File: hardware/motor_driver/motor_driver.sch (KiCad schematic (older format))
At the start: 37 parts, among them P1 TERM_BLOCK_CON, P2 JUMPER_CIRC_SUPLLY, P3 TERM_BLOCK_CON, P4 FEMALE_HEADER, P5 MOLEX_HEADER, Q1 IRFZ40, Q2 IRFZ40, Q3 IRFZ40, Q4 IRFZ40, U1 LM7812, U2 LM7805, U3 HIP4081A, U4 SN74S04

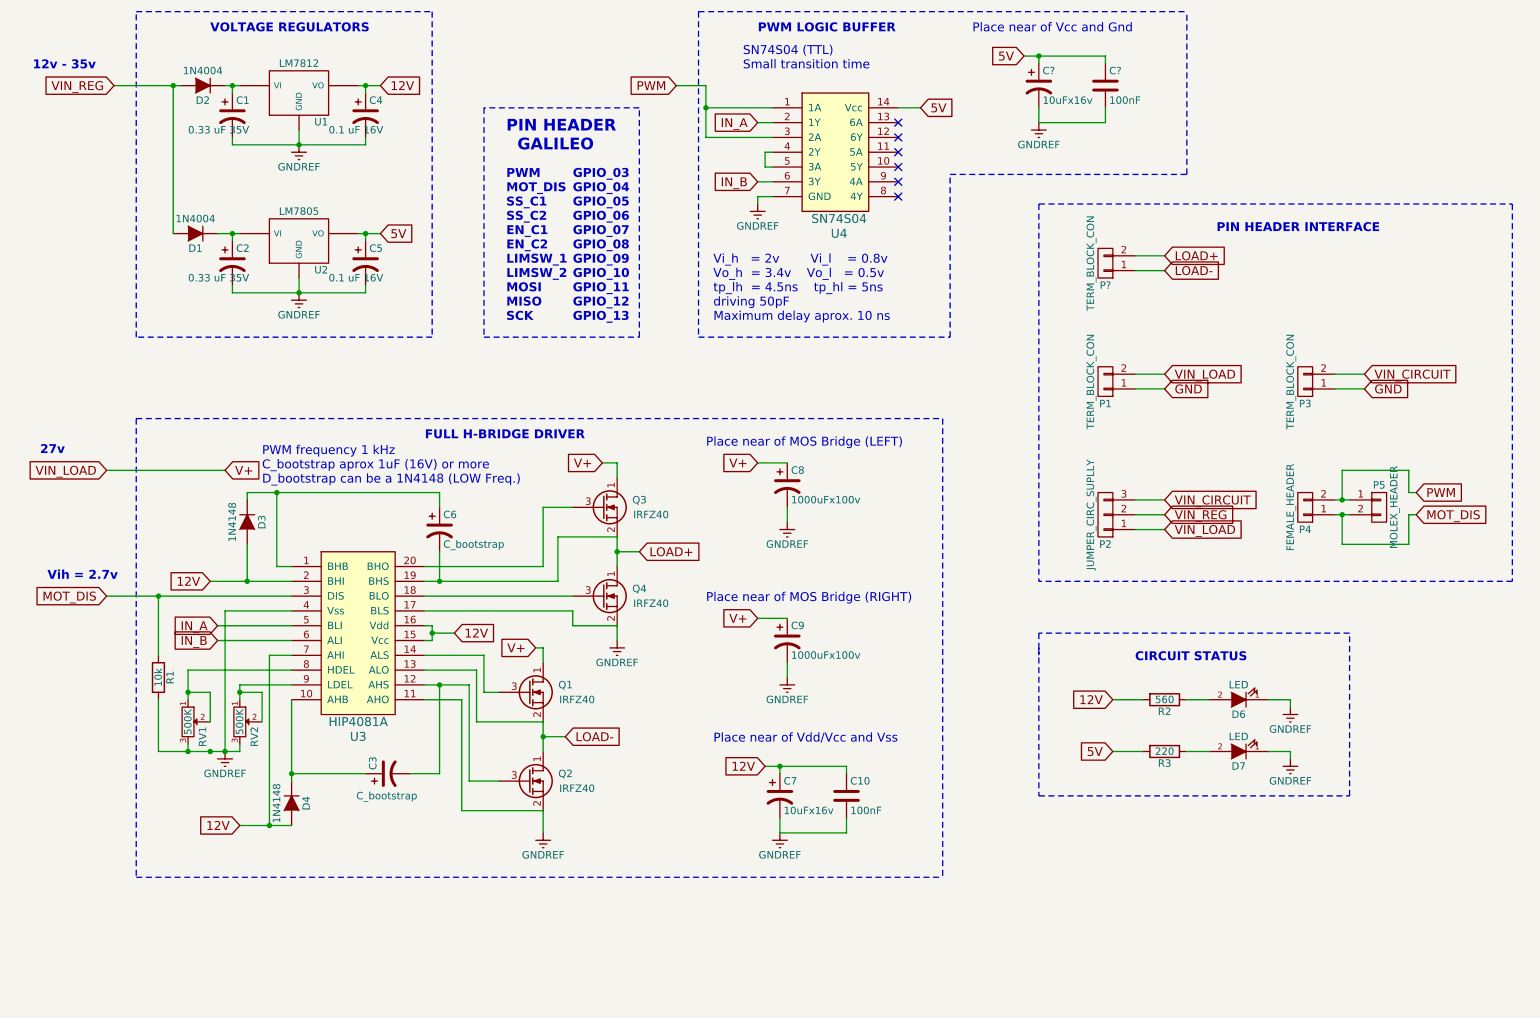
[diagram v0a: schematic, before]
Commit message: Added PID, LS7366R lib and layout off DC Motor Driver PCB and Arduino Shied PCB.
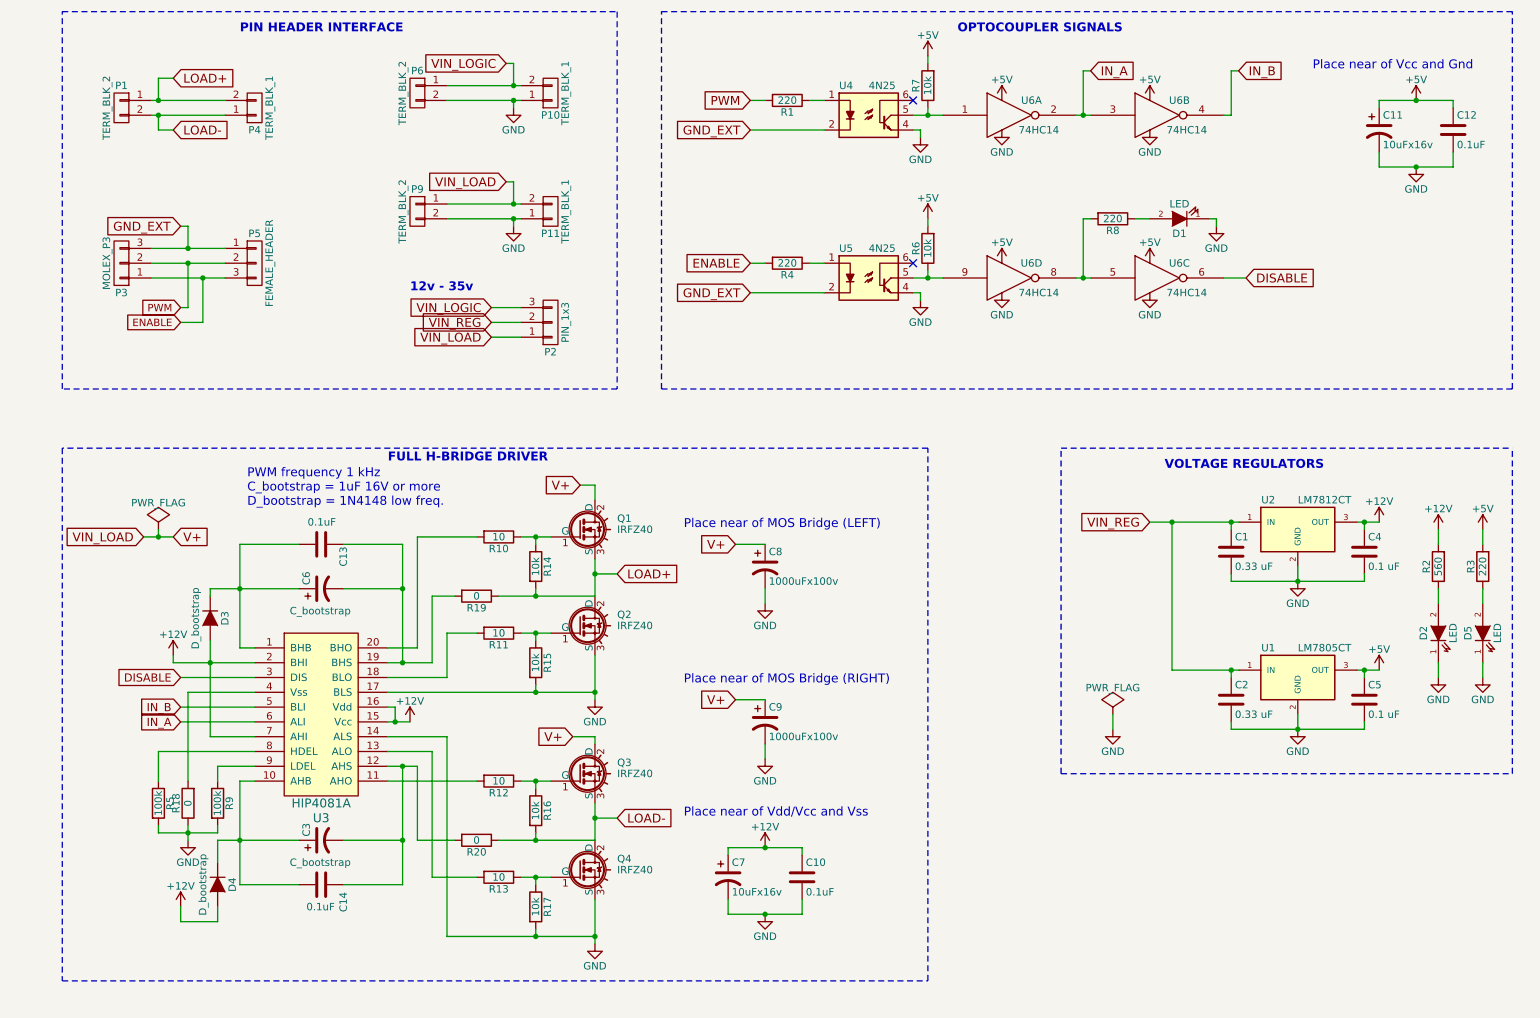
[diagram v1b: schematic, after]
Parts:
- removed C1, C2: 0.33 uF 35V, symbol CP1
- removed C4, C5: 0.1 uF 16V, symbol CP1
- removed D1, D2: 1N4004, symbol D
- removed D6, D7: LED, symbol LED
- removed P3, P?: TERM_BLOCK_CON, symbol CONN_01X02
- removed P5: MOLEX_HEADER, symbol CONN_01X02
- removed Q1, Q2, Q3, Q4: IRFZ40, symbol Q_NMOS_DSG
- removed RV1, RV2: 500K, symbol POT
- removed U1: LM7812, symbol LM7812
- removed U2: LM7805, symbol LM7805
- removed U4: SN74S04, symbol SN74S04
- added C1, C2: 0.33 uF, Maplex_Misc:C_Disc_D7.5mm_W2.5mm_P5.00mm, symbol C
- added C13, C14: 0.1uF, Maplex_Misc:C_Disc_D5.0mm_W2.5mm_P2.50mm, symbol C
- added C4, C5: 0.1 uF, Maplex_Misc:C_Disc_D5.0mm_W2.5mm_P2.50mm, symbol C
- added D1, D2, D5: LED, Maplex_Misc:LED_D5.0mm, symbol LED
- added P10, P11: TERM_BLK_1, Maplex_Misc:TerminalBlock_2Pin_P5.08mm_L9mm, symbol CONN_01X02
- added P3: MOLEX_P3, Maplex_Misc:Molex_3Pin_180_TH, symbol CONN_01X03
- added P5: FEMALE_HEADER, Maplex_Misc:Pin_Header_Straight_1x03_Pitch2.54mm, symbol CONN_01X03
- added P6, P9: TERM_BLK_2, Maplex_Misc:TerminalBlock_2Pin_P5.08mm_L12mm, symbol CONN_01X02
- added Q1, Q2, Q3, Q4: IRFZ40, Maplex_Misc:TO-220_Neutral_Vertical, symbol IRF540N
- added R10, R11, R12, R13: 10, Maplex_Misc:Resistor_Horizontal_RM10mm_L7mm, symbol R
- added R14, R15, R16, R17, R6, R7: 10k, Maplex_Misc:Resistor_Horizontal_RM10mm_L7mm, symbol R
- added R18, R19, R20: 0, Maplex_Misc:Resistor_Horizontal_RM10mm_L7mm, symbol R
- added R4, R8: 220, Maplex_Misc:Resistor_Horizontal_RM10mm_L7mm, symbol R
- added R5, R9: 100k, Maplex_Misc:Resistor_Horizontal_RM10mm_L7mm, symbol R
- added U1: LM7805CT, Maplex_Misc:TO-220_Neutral_Vertical, symbol LM7805CT
- added U2: LM7812CT, Maplex_Misc:TO-220_Neutral_Vertical, symbol LM7812CT
- added U4, U5: 4N25, Maplex_Misc:DIP-6_W7.62mm_Socket, symbol 4N25
- added U6: 74HC14, Maplex_Misc:DIP-14_W7.62mm_Socket, symbol 74HC14
- C10: value 100nF -> 0.1uF; footprint (none) -> Maplex_Misc:C_Disc_D5.0mm_W2.5mm_P2.50mm
- C11: renamed from C?; footprint (none) -> Maplex_Misc:CP_Radial_D6.3mm_P2.50mm
- C12: renamed from C?; value 100nF -> 0.1uF; footprint (none) -> Maplex_Misc:C_Disc_D5.0mm_W2.5mm_P2.50mm
- C3, C6, C7: footprint (none) -> Maplex_Misc:CP_Radial_D6.3mm_P2.50mm
- C8, C9: footprint (none) -> Maplex_Misc:CP_Radial_D12.5mm_P5.00mm
- D3, D4: value 1N4148 -> D_bootstrap; footprint (none) -> Maplex_Misc:Diode_P7.6mm_5mm
- P1: value TERM_BLOCK_CON -> TERM_BLK_2; footprint (none) -> Maplex_Misc:TerminalBlock_2Pin_P5.08mm_L12mm
- P2: value JUMPER_CIRC_SUPLLY -> PIN_1x3; footprint (none) -> Maplex_Misc:Pin_Header_Straight_1x03_Pitch2.54mm
- P4: value FEMALE_HEADER -> TERM_BLK_1; footprint (none) -> Maplex_Misc:TerminalBlock_2Pin_P5.08mm_L9mm
- R1: value 10k -> 220; footprint (none) -> Maplex_Misc:Resistor_Horizontal_RM10mm_L7mm
- R2, R3: footprint (none) -> Maplex_Misc:Resistor_Horizontal_RM10mm_L7mm
- U3: footprint (none) -> Maplex_Misc:DIP-20_W7.62mm_Socket
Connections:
- net GND: now also C10.2, C11.2, C12.2, C7.2, C8.2, C9.2, U3.14 (ALS), U3.17 (BLS), C1.2, C2.2, C4.2, C5.2, D1.1 (K), D2.1 (K), D5.1 (K), P10.1 (P1), P11.1 (P1), P6.2 (P2), P9.2 (P2), Q2.3 (S), Q4.3 (S), R15.2, R17.2, R18.1, R5.2, R9.2, U1.2 (GND), U2.2 (GND), U4.4, U5.4, U6.7 (GND), U6.7 (GND), U6.7 (GND), U6.7 (GND); no longer P1.1 (P1)
- net IN_A: now also U3.6 (ALI), U6.2, U6.3; no longer U3.5 (BLI)
- net IN_B: now also U3.5 (BLI), U6.4; no longer U3.6 (ALI)
- net LOAD+: now also P1.1 (P1), P4.2 (P2), Q1.3 (S), Q2.2 (D), R14.2, R19.1; no longer C6.2, U3.19 (BHS)
- net LOAD-: now also P1.2 (P2), P4.1 (P1), Q3.3 (S), Q4.2 (D), R16.2, R20.1; no longer U3.13 (ALO)
- net PWM: now also R1.2, P3.2 (P2), P5.2 (P2); no longer P4.2 (P2)
- net V+: now also P11.2 (P2), P9.1 (P1), Q1.2 (D), Q3.2 (D); no longer P1.2 (P2)
- net VIN_REG: now also C1.1, C2.1, U1.1 (IN), U2.1 (IN)
- net at U3.20 (BHO): now also R10.2
- net at U3.18 (BLO): now also R11.2
- net at C3.2, U3.12 (AHS): now also C14.1, R20.2
- net at C6.1, D3.1 (K), U3.1 (BHB): now also C13.1
- net at C3.1, D4.1 (K), U3.10 (AHB): now also C14.2
- net at U3.8 (HDEL): now also R5.1
- net at U3.9 (LDEL): now also R9.1
- net at R2.1: now also D2.2 (A)
- net at R3.1: now also D5.2 (A)
- net 12V renamed +12V
- net +12V: now also C4.1, U2.3 (OUT)
- net 5V renamed +5V
- net +5V: now also C5.1, R6.2, R7.2, U1.3 (OUT), U6.14 (VCC), U6.14 (VCC), U6.14 (VCC), U6.14 (VCC)
- removed net GNDREF: C10.2, C11.2, C12.2, C7.2, C8.2, C9.2, R1.2, U3.11 (AHO), U3.17 (BLS), U3.4 (Vss)
- removed net MOT_DIS: P4.1 (P1), R1.1, U3.3 (DIS)
- net VIN_CIRCUIT renamed VIN_LOGIC
- net VIN_LOGIC: now also P10.2 (P2), P6.1 (P1)
- new net: R12.2, U3.11 (AHO)
- new net: R13.2, U3.13 (ALO)
- new net: C13.2, C6.2, R19.2, U3.19 (BHS)
- new net: R18.2, U3.4 (Vss)
- new net: R1.1, U4.1
- new net: R7.1, U4.5, U6.1
- new net: R4.1, U5.1
- new net: R6.1, U5.5, U6.9
- new net: R8.2, U6.5, U6.8
- new net: D1.2 (A), R8.1
- new net: Q1.1 (G), R10.1, R14.1
- new net: Q3.1 (G), R12.1, R16.1
- new net: Q2.1 (G), R11.1, R15.1
- new net: Q4.1 (G), R13.1, R17.1
- new net DISABLE: U3.3 (DIS), U6.6
- new net ENABLE: P3.1 (P1), P5.3 (P3), R4.2
- new net GND_EXT: P3.3 (P3), P5.1 (P1), U4.2, U5.2
- no-connect marks 6 -> 2
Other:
- note added: "OPTOCOUPLER SIGNALS"
- note added: "PWM frequency 1 kHz\nC_bootstrap = 1uF 16V or more\nD_bootstrap = 1N4148 low freq."
- note removed: "27v"
- note removed: "CIRCUIT STATUS"
- note removed: "GPIO_03\nGPIO_04\nGPIO_05\nGPIO_06\nGPIO_07\nGPIO_08\nGPIO_09\nGPIO_10\nGPIO_11\nGPIO_12\nGPIO_13"
- note removed: "PIN HEADER\n GALILEO"
- note removed: "PWM LOGIC BUFFER\n"
- note removed: "PWM frequency 1 kHz\nC_bootstrap aprox 1uF (16V) or more\nD_bootstrap can be a 1N4148 (LOW Freq.)"
- note removed: "PWM\nMOT_DIS\nSS_C1\nSS_C2\nEN_C1\nEN_C2\nLIMSW_1\nLIMSW_2\nMOSI\nMISO\nSCK"
- note removed: "SN74S04 (TTL)\nSmall transition time"
- note removed: "Vi_h = 2v Vi_l = 0.8v\nVo_h = 3.4v Vo_l = 0.5v\ntp_lh = 4.5ns tp_hl = 5ns\ndriving 50pF\nMaximum delay aprox. 10 ns"
- note removed: "Vih = 2.7v"
- moved on the sheet: C10, C11, C12, C3, C6, C7, C8, C9, D3, D4, P2, R2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

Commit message: Last version.
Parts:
- removed P1, P6, P9: TERM_BLK_2, Maplex_Misc:TerminalBlock_2Pin_P5.08mm_L12mm, symbol CONN_01X02
- removed P10, P11, P4: TERM_BLK_1, Maplex_Misc:TerminalBlock_2Pin_P5.08mm_L9mm, symbol CONN_01X02
- removed P2: PIN_1x3, Maplex_Misc:Pin_Header_Straight_1x03_Pitch2.54mm, symbol CONN_01X03
- removed P3: MOLEX_P3, Maplex_Misc:Molex_3Pin_180_TH, symbol CONN_01X03
- removed P5: FEMALE_HEADER, Maplex_Misc:Pin_Header_Straight_1x03_Pitch2.54mm, symbol CONN_01X03
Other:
- note added: "02/07/17"
- note added: "DC Motor Driver with PWM"
- note removed: "12v - 35v"
- note removed: "PIN HEADER INTERFACE"
- moved on the sheet: C11, C12, D1, R1, R4, R6, R7, R8, U4, U5, U6A, U6B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
